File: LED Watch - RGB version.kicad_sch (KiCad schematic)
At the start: 186 parts, among them Q1 BD135, Q10 BD135, Q11 BD135, Q12 BD135, Q13 BD135, Q2 BD135, Q3 BD135, Q4 BD135, Q5 BD135, Q6 BD135, Q7 BD135, Q8 BD135, Q9 BD135, U1 ATMEGA32U4-AU, U10 74LVC2G08, U11 74LVC2G08, U12 74LVC2G08, U13 74LVC2G08, U14 74LVC2G08, U15 74LVC2G08, U16 74LVC2G08, U17 74LVC2G08, U18 74LVC2G08, U19 74LVC2G08, U2 74LVC2G08, U20 74LVC2G08, U21 74LVC2G08, U22 74LVC2G08, U23 74LVC2G08, U24 74LVC2G08, U25 74LVC2G08, U26 74LVC2G08, U27 74LVC2G08, U28 74LVC2G08, U29 74LVC2G08, U3 74LVC2G08, U30 74LVC2G08, U31 74LVC2G08, U32 74LVC2G08, U33 74LVC2G08, U34 74LVC2G08, U35 74LVC2G08, U36 74LVC2G08, U37 74LVC2G08, U38 74LVC2G08, U39 74LVC2G08, U4 74LVC2G08, U40 74LVC2G08, U41 74LVC2G08, U5 74LVC2G08, U6 74LVC2G08, U7 74LVC2G08, U8 74LVC2G08, U9 74LVC2G08

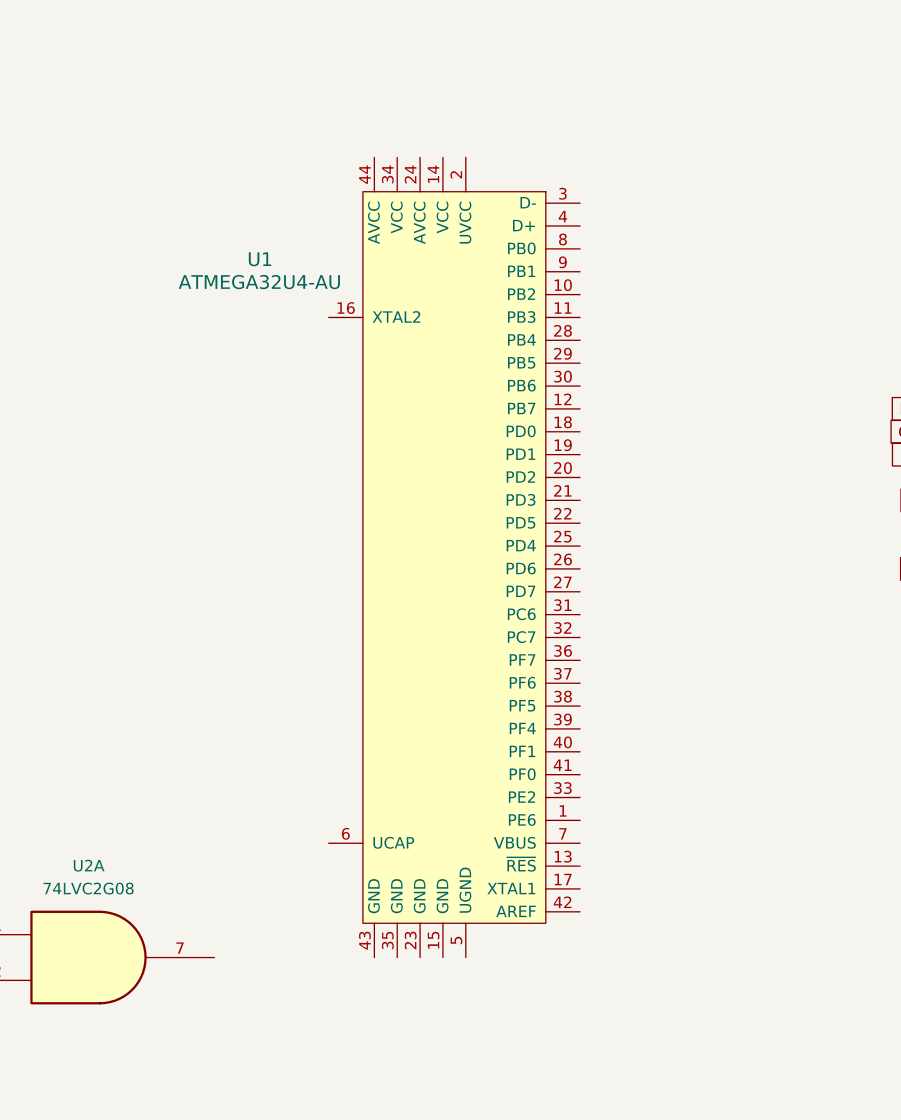
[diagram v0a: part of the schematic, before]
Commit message: chip swap to atmega4808
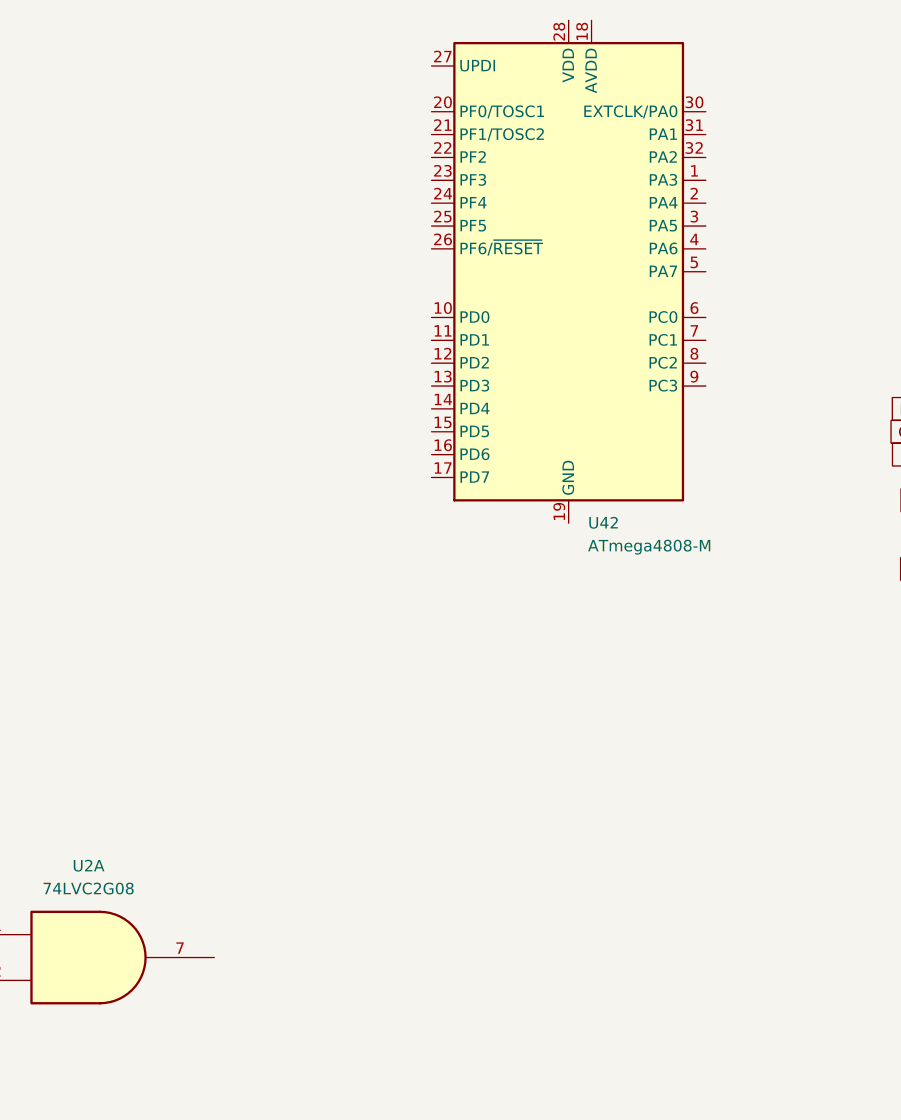
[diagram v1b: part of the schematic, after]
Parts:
- removed U1: ATMEGA32U4-AU, digikey-footprints:TQFP-44_10x10mm, symbol dk_Embedded-Microcontrollers:ATMEGA32U4-AU
- added U42: ATmega4808-M, Package_DFN_QFN:QFN-32-1EP_5x5mm_P0.5mm_EP3.1x3.1mm_ThermalVias, symbol MCU_Microchip_ATmega:ATmega4808-M
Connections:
- new net: U42.19 (GND), U42.29 (GND), U42.33 (GND)
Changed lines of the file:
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@@
 	)
 	(symbol
-		(lib_id "dk_Embedded-Microcontrollers:ATMEGA32U4-AU")
-		(at 74.93 104.14 0)
-		(mirror y)
-		(unit 1)
-		(exclude_from_sim no)
-		(in_bom yes)
-		(on_board yes)
-		(dnp no)
-		(property "Reference" "U1"
-			(at 54.61 77.3998 0)
-			(effects
-				(font
-					(size 1.524 1.524)
-				)
-			)
-		)
-		(property "Value" "ATMEGA32U4-AU"
-			(at 54.61 79.9398 0)
-			(effects
-				(font
-					(size 1.524 1.524)
-				)
-			)
-		)
-		(property "Footprint" "digikey-footprints:TQFP-44_10x10mm"
-			(at 69.85 99.06 0)
-			(effects
-				(font
-					(size 1.524 1.524)
-				)
-				(justify left)
-				(hide yes)
-			)
-		)
-		(property "Datasheet" "http://ww1.microchip.com/downloads/en/DeviceDoc/Atmel-7766-8-bit-AVR-ATmega16U4-32U4_Summary.pdf"
-			(at 69.85 96.52 0)
-			(effects
-				(font
-					(size 1.524 1.524)
-				)
-				(justify left)
-				(hide yes)
-			)
-		)
-		(property "Description" "IC MCU 8BIT 32KB FLASH 44TQFP"
-			(at 74.93 104.14 0)
-			(effects
-				(font
-					(size 1.27 1.27)
-				)
-				(hide yes)
-			)
-		)
-		(property "Digi-Key_PN" "ATMEGA32U4-AU-ND"
-			(at 69.85 93.98 0)
-			(effects
-				(font
-					(size 1.524 1.524)
-				)
-				(justify left)
-				(hide yes)
-			)
-		)
-		(property "MPN" "ATMEGA32U4-AU"
-			(at 69.85 91.44 0)
-			(effects
-				(font
-					(size 1.524 1.524)
-				)
-				(justify left)
-				(hide yes)
-			)
-		)
-		(property "Category" "Integrated Circuits (ICs)"
-			(at 69.85 88.9 0)
-			(effects
-				(font
-					(size 1.524 1.524)
-				)
-				(justify left)
-				(hide yes)
-			)
-		)
-		(property "Family" "Embedded - Microcontrollers"
-			(at 69.85 86.36 0)
-			(effects
-				(font
-					(size 1.524 1.524)
-				)
-				(justify left)
-				(hide yes)
-			)
-		)
-		(property "DK_Datasheet_Link" "http://ww1.microchip.com/downloads/en/DeviceDoc/Atmel-7766-8-bit-AVR-ATmega16U4-32U4_Summary.pdf"
-			(at 69.85 83.82 0)
-			(effects
-				(font
-					(size 1.524 1.524)
-				)
-				(justify left)
-				(hide yes)
-			)
-		)
-		(property "DK_Detail_Page" "/product-detail/en/microchip-technology/ATMEGA32U4-AU/ATMEGA32U4-AU-ND/1914602"
-			(at 69.85 81.28 0)
-			(effects
-				(font
-					(size 1.524 1.524)
-				)
-				(justify left)
-				(hide yes)
-			)
-		)
-		(property "Description_1" "IC MCU 8BIT 32KB FLASH 44TQFP"
-			(at 69.85 78.74 0)
-			(effects
-				(font
-					(size 1.524 1.524)
-				)
-				(justify left)
-				(hide yes)
-			)
-		)
-		(property "Manufacturer" "Microchip Technology"
-			(at 69.85 76.2 0)
-			(effects
-				(font
-					(size 1.524 1.524)
-				)
-				(justify left)
-				(hide yes)
-			)
-		)
-		(property "Status" "Active"
-			(at 69.85 73.66 0)
-			(effects
-				(font
-					(size 1.524 1.524)
-				)
-				(justify left)
-				(hide yes)
-			)
-		)
-		(pin "18"
-		)
-		(pin "3"
-		)
-		(pin "11"
-		)
-		(pin "8"
-		)
-		(pin "28"
-		)
-		(pin "4"
-		)
-		(pin "29"
-		)
-		(pin "30"
-		)
-		(pin "9"
-		)
-		(pin "10"
-		)
-		(pin "12"
-		)
-		(pin "41"
-		)
-		(pin "13"
-		)
-		(pin "26"
-		)
-		(pin "36"
-		)
-		(pin "22"
-		)
-		(pin "31"
-		)
-		(pin "19"
-		)
-		(pin "21"
-		)
-		(pin "20"
-		)
-		(pin "27"
-		)
-		(pin "32"
-		)
-		(pin "38"
-		)
-		(pin "40"
-		)
-		(pin "7"
-		)
-		(pin "24"
-		)
-		(pin "39"
-		)
-		(pin "14"
-		)
-		(pin "5"
-		)
-		(pin "25"
-		)
-		(pin "37"
-		)
-		(pin "33"
-		)
-		(pin "1"
-		)
-		(pin "42"
-		)
-		(pin "44"
-		)
-		(pin "35"
-		)
-		(pin "2"
-		)
-		(pin "43"
-		)
-		(pin "23"
-		)
-		(pin "16"
-		)
-		(pin "15"
-		)
-		(pin "17"
-		)
-		(pin "34"
-		)
-		(pin "6"
-		)
-		(instances
-			(project ""
-				(path "/4f6e3ccb-61a7-41db-9176-b9c2e62eec38"
-					(reference "U1")
-					(unit 1)
-				)
-			)
-		)
-	)
-	(symbol
 		(lib_id "dk_LED-Indication-Discrete:LTST-C19HE1WT")
 		(at 281.94 134.62 0)
@@
 					(unit 1)
 				)
+			)
+		)
+	)
+	(symbol
+		(lib_id "MCU_Microchip_ATmega:ATmega4808-M")
+		(at 88.9 78.74 0)
+		(unit 1)
+		(exclude_from_sim no)
+		(in_bom yes)
+		(on_board yes)
+		(dnp no)
+		(fields_autoplaced yes)
+		(property "Reference" "U42"
+			(at 91.0433 106.68 0)
+			(effects
+				(font
+					(size 1.27 1.27)
+				)
+				(justify left)
+			)
+		)
+		(property "Value" "ATmega4808-M"
+			(at 91.0433 109.22 0)
+			(effects
+				(font
+					(size 1.27 1.27)
+				)
+				(justify left)
+			)
+		)
+		(property "Footprint" "Package_DFN_QFN:QFN-32-1EP_5x5mm_P0.5mm_EP3.1x3.1mm_ThermalVias"
+			(at 88.9 78.74 0)
+			(effects
+				(font
+					(size 1.27 1.27)
+					(italic yes)
+				)
+				(hide yes)
+			)
+		)
+		(property "Datasheet" "http://ww1.microchip.com/downloads/en/DeviceDoc/40002017A.pdf"
+			(at 88.9 78.74 0)
+			(effects
+				(font
+					(size 1.27 1.27)
+				)
+				(hide yes)
+			)
+		)
+		(property "Description" "20MHz, 48kB Flash, 6kB SRAM, 256B EEPROM, VQFN-32"
+			(at 88.9 78.74 0)
+			(effects
+				(font
+					(size 1.27 1.27)
+				)
+				(hide yes)
+			)
+		)
+		(pin "28"
+		)
+		(pin "10"
+		)
+		(pin "15"
+		)
+		(pin "23"
+		)
+		(pin "17"
+		)
+		(pin "27"
+		)
+		(pin "26"
+		)
+		(pin "11"
+		)
+		(pin "16"
+		)
+		(pin "21"
+		)
+		(pin "25"
+		)
+		(pin "13"
+		)
+		(pin "12"
+		)
+		(pin "4"
+		)
+		(pin "22"
+		)
+		(pin "24"
+		)
+		(pin "20"
+		)
+		(pin "14"
+		)
+		(pin "18"
+		)
+		(pin "5"
+		)
+		(pin "30"
+		)
+		(pin "19"
+		)
+		(pin "31"
+		)
+		(pin "32"
+		)
+		(pin "1"
+		)
+		(pin "6"
+		)
+		(pin "33"
+		)
+		(pin "3"
+		)
+		(pin "8"
+		)
+		(pin "7"
+		)
+		(pin "29"
+		)
+		(pin "2"
+		)
+		(pin "9"
+		)
+		(instances
+			(project ""
+				(path "/4f6e3ccb-61a7-41db-9176-b9c2e62eec38"
+					(reference "U42")
+					(unit 1)
+				)

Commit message: added bus bars. things are where i think they should be but i need to double check transistors and do a lot more
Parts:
- removed Q1, Q10, Q11, Q12, Q13, Q2, Q3, Q4, Q5, Q6, Q7, Q8, Q9: BD135, Package_TO_SOT_THT:TO-126-3_Vertical, symbol Transistor_BJT:BD135
- removed RGB_LED126, RGB_LED127, RGB_LED128, RGB_LED129, RGB_LED138, RGB_LED139, RGB_LED140, RGB_LED141: LTST-C19HE1WT, digikey-footprints:LED_Dual0603, symbol dk_LED-Indication-Discrete:LTST-C19HE1WT
- removed U10, U11, U12, U13, U14, U15, U16, U17, U18, U19, U2, U20, U21, U22, U23, U24, U25, U26, U27, U28, U29, U3, U30, U31, U32, U33, U34, U35, U36, U37, U38, U39, U4, U40, U41, U5, U6, U7, U8, U9: 74LVC2G08, symbol 74xGxx:74LVC2G08
- removed U42: ATmega4808-M, Package_DFN_QFN:QFN-32-1EP_5x5mm_P0.5mm_EP3.1x3.1mm_ThermalVias, symbol MCU_Microchip_ATmega:ATmega4808-M
- added Q23, Q24, Q25, Q26, Q27, Q28, Q29, Q30, Q31, Q32, Q33, Q34, Q35, Q36, Q37, Q38, Q39, Q40, Q41, Q42, Q43, Q44: BD135, Package_TO_SOT_THT:TO-126-3_Vertical, symbol Transistor_BJT:BD135
- added RGB_LED10, RGB_LED3, RGB_LED6, RGB_LED7, RGB_LED8, RGB_LED9, RGB_LED94, RGB_LED95: LTST-C19HE1WT, digikey-footprints:LED_Dual0603, symbol dk_LED-Indication-Discrete:LTST-C19HE1WT
- added U1: ATmega165PA-A, Package_QFP:TQFP-64_14x14mm_P0.8mm, symbol MCU_Microchip_ATmega:ATmega165PA-A
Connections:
- net VCC: now also Q23.3 (B), Q24.3 (B), Q25.3 (B), Q26.3 (B), Q27.3 (B), Q28.3 (B), Q29.3 (B), Q30.3 (B), Q31.3 (B), Q32.3 (B), Q33.3 (B), Q34.3 (B), Q35.3 (B), Q36.3 (B), Q37.3 (B), Q38.3 (B), Q39.3 (B), Q40.3 (B), Q41.3 (B), Q42.3 (B), Q43.3 (B), Q44.3 (B)
- net at RGB_LED22.4, RGB_LED23.4, RGB_LED34.4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: now also Q36.2 (C); no longer RGB_LED58.4, RGB_LED59.4, RGB_LED70.4, RGB_LED71.4
- net R4: now reaches RGB_LED51.1 (R)
- net R4: now also RGB_LED111.1 (R), RGB_LED115.1 (R), RGB_LED119.1 (R), RGB_LED123.1 (R), RGB_LED135.1 (R), RGB_LED15.1 (R), RGB_LED21.1 (R), RGB_LED27.1 (R), RGB_LED35.1 (R), RGB_LED39.1 (R), RGB_LED43.1 (R), RGB_LED57.1 (R), RGB_LED63.1 (R), RGB_LED69.1 (R), RGB_LED75.1 (R), RGB_LED81.1 (R), RGB_LED83.1 (R), RGB_LED87.1 (R), RGB_LED99.1 (R), RGB_LED8.1 (R), RGB_LED95.1 (R), U1.11 (PB1)
- net G4: now reaches RGB_LED51.2 (G)
- net G4: now also RGB_LED111.2 (G), RGB_LED115.2 (G), RGB_LED119.2 (G), RGB_LED123.2 (G), RGB_LED135.2 (G), RGB_LED15.2 (G), RGB_LED21.2 (G), RGB_LED27.2 (G), RGB_LED35.2 (G), RGB_LED39.2 (G), RGB_LED43.2 (G), RGB_LED57.2 (G), RGB_LED63.2 (G), RGB_LED69.2 (G), RGB_LED75.2 (G), RGB_LED81.2 (G), RGB_LED83.2 (G), RGB_LED87.2 (G), RGB_LED99.2 (G), RGB_LED8.2 (G), RGB_LED95.2 (G), U1.12 (PB2)
- net B4: now reaches RGB_LED51.3 (B)
- net B4: now also RGB_LED111.3 (B), RGB_LED115.3 (B), RGB_LED119.3 (B), RGB_LED123.3 (B), RGB_LED135.3 (B), RGB_LED15.3 (B), RGB_LED21.3 (B), RGB_LED27.3 (B), RGB_LED35.3 (B), RGB_LED39.3 (B), RGB_LED43.3 (B), RGB_LED57.3 (B), RGB_LED63.3 (B), RGB_LED69.3 (B), RGB_LED75.3 (B), RGB_LED81.3 (B), RGB_LED83.3 (B), RGB_LED87.3 (B), RGB_LED99.3 (B), RGB_LED8.3 (B), RGB_LED95.3 (B), U1.13 (PB3)
- net at RGB_LED48.4, RGB_LED49.4, RGB_LED50.4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: now also Q28.2 (C); no longer RGB_LED54.4, RGB_LED55.4, RGB_LED56.4, RGB_LED57.4
- net at RGB_LED72.4, RGB_LED73.4, RGB_LED74.4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: now also Q30.2 (C); no longer RGB_LED78.4, RGB_LED79.4, RGB_LED80.4, RGB_LED81.4
- net at RGB_LED120.4, RGB_LED121.4, RGB_LED122.4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: now also Q34.2 (C)
- net R1: now reaches RGB_LED92.1 (R)
- net R1: now also RGB_LED.1 (R), RGB_LED104.1 (R), RGB_LED106.1 (R), RGB_LED108.1 (R), RGB_LED12.1 (R), RGB_LED120.1 (R), RGB_LED132.1 (R), RGB_LED18.1 (R), RGB_LED22.1 (R), RGB_LED24.1 (R), RGB_LED32.1 (R), RGB_LED36.1 (R), RGB_LED48.1 (R), RGB_LED54.1 (R), RGB_LED60.1 (R), RGB_LED66.1 (R), RGB_LED72.1 (R), RGB_LED78.1 (R), RGB_LED84.1 (R), RGB_LED96.1 (R), RGB_LED3.1 (R), U1.51 (PA0)
- net G1: now reaches RGB_LED92.2 (G)
- net G1: now also RGB_LED.2 (G), RGB_LED104.2 (G), RGB_LED106.2 (G), RGB_LED108.2 (G), RGB_LED12.2 (G), RGB_LED120.2 (G), RGB_LED132.2 (G), RGB_LED18.2 (G), RGB_LED22.2 (G), RGB_LED24.2 (G), RGB_LED32.2 (G), RGB_LED36.2 (G), RGB_LED48.2 (G), RGB_LED54.2 (G), RGB_LED60.2 (G), RGB_LED66.2 (G), RGB_LED72.2 (G), RGB_LED78.2 (G), RGB_LED84.2 (G), RGB_LED96.2 (G), RGB_LED3.2 (G), U1.50 (PA1)
- net B1: now reaches RGB_LED92.3 (B)
- net B1: now also RGB_LED.3 (B), RGB_LED104.3 (B), RGB_LED106.3 (B), RGB_LED108.3 (B), RGB_LED12.3 (B), RGB_LED120.3 (B), RGB_LED132.3 (B), RGB_LED18.3 (B), RGB_LED22.3 (B), RGB_LED24.3 (B), RGB_LED32.3 (B), RGB_LED36.3 (B), RGB_LED48.3 (B), RGB_LED54.3 (B), RGB_LED60.3 (B), RGB_LED66.3 (B), RGB_LED72.3 (B), RGB_LED78.3 (B), RGB_LED84.3 (B), RGB_LED96.3 (B), RGB_LED3.3 (B), U1.49 (PA2)
- net at RGB_LED84.4, RGB_LED85.4, RGB_LED86.4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: now also Q31.2 (C); no longer RGB_LED90.4, RGB_LED91.4, RGB_LED92.4, RGB_LED93.4
- net at RGB_LED12.4, RGB_LED13.4, RGB_LED14.4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: now also Q25.2 (C); no longer RGB_LED18.4, RGB_LED19.4, RGB_LED20.4, RGB_LED21.4
- net R5: now reaches RGB_LED112.1 (R)
- net R5: now also RGB_LED100.1 (R), RGB_LED102.1 (R), RGB_LED116.1 (R), RGB_LED124.1 (R), RGB_LED136.1 (R), RGB_LED16.1 (R), RGB_LED2.1 (R), RGB_LED28.1 (R), RGB_LED30.1 (R), RGB_LED4.1 (R), RGB_LED40.1 (R), RGB_LED44.1 (R), RGB_LED46.1 (R), RGB_LED52.1 (R), RGB_LED58.1 (R), RGB_LED64.1 (R), RGB_LED70.1 (R), RGB_LED76.1 (R), RGB_LED88.1 (R), RGB_LED90.1 (R), RGB_LED9.1 (R), U1.14 (PB4)
- net G5: now reaches RGB_LED112.2 (G)
- net G5: now also RGB_LED100.2 (G), RGB_LED102.2 (G), RGB_LED116.2 (G), RGB_LED124.2 (G), RGB_LED136.2 (G), RGB_LED16.2 (G), RGB_LED2.2 (G), RGB_LED28.2 (G), RGB_LED30.2 (G), RGB_LED4.2 (G), RGB_LED40.2 (G), RGB_LED44.2 (G), RGB_LED46.2 (G), RGB_LED52.2 (G), RGB_LED58.2 (G), RGB_LED64.2 (G), RGB_LED70.2 (G), RGB_LED76.2 (G), RGB_LED88.2 (G), RGB_LED90.2 (G), RGB_LED9.2 (G), U1.15 (PB5)
- net B5: now reaches RGB_LED112.3 (B)
- net B5: now also RGB_LED100.3 (B), RGB_LED102.3 (B), RGB_LED116.3 (B), RGB_LED124.3 (B), RGB_LED136.3 (B), RGB_LED16.3 (B), RGB_LED2.3 (B), RGB_LED28.3 (B), RGB_LED30.3 (B), RGB_LED4.3 (B), RGB_LED40.3 (B), RGB_LED44.3 (B), RGB_LED46.3 (B), RGB_LED52.3 (B), RGB_LED58.3 (B), RGB_LED64.3 (B), RGB_LED70.3 (B), RGB_LED76.3 (B), RGB_LED88.3 (B), RGB_LED90.3 (B), RGB_LED9.3 (B), U1.16 (PB6)
- net at RGB_LED108.4, RGB_LED109.4, RGB_LED110.4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: now also Q33.2 (C); no longer RGB_LED114.4, RGB_LED115.4, RGB_LED116.4, RGB_LED117.4
- net R6: now reaches RGB_LED11.1 (R)
- net R6: now also RGB_LED101.1 (R), RGB_LED103.1 (R), RGB_LED113.1 (R), RGB_LED117.1 (R), RGB_LED125.1 (R), RGB_LED137.1 (R), RGB_LED17.1 (R), RGB_LED29.1 (R), RGB_LED31.1 (R), RGB_LED41.1 (R), RGB_LED45.1 (R), RGB_LED47.1 (R), RGB_LED5.1 (R), RGB_LED53.1 (R), RGB_LED59.1 (R), RGB_LED65.1 (R), RGB_LED71.1 (R), RGB_LED77.1 (R), RGB_LED89.1 (R), RGB_LED91.1 (R), RGB_LED10.1 (R), U1.17 (PB7)
- net B2: now reaches RGB_LED1.3 (B)
- net B2: now also RGB_LED105.3 (B), RGB_LED107.3 (B), RGB_LED109.3 (B), RGB_LED121.3 (B), RGB_LED13.3 (B), RGB_LED133.3 (B), RGB_LED19.3 (B), RGB_LED23.3 (B), RGB_LED25.3 (B), RGB_LED33.3 (B), RGB_LED37.3 (B), RGB_LED49.3 (B), RGB_LED55.3 (B), RGB_LED61.3 (B), RGB_LED67.3 (B), RGB_LED73.3 (B), RGB_LED79.3 (B), RGB_LED85.3 (B), RGB_LED93.3 (B), RGB_LED97.3 (B), RGB_LED6.3 (B), U1.46 (PA5)
- net R3: now reaches RGB_LED38.1 (R)
- net R3: now also RGB_LED110.1 (R), RGB_LED114.1 (R), RGB_LED118.1 (R), RGB_LED122.1 (R), RGB_LED134.1 (R), RGB_LED14.1 (R), RGB_LED20.1 (R), RGB_LED26.1 (R), RGB_LED34.1 (R), RGB_LED42.1 (R), RGB_LED50.1 (R), RGB_LED56.1 (R), RGB_LED62.1 (R), RGB_LED68.1 (R), RGB_LED74.1 (R), RGB_LED80.1 (R), RGB_LED82.1 (R), RGB_LED86.1 (R), RGB_LED98.1 (R), RGB_LED7.1 (R), RGB_LED94.1 (R), U1.45 (PA6)
- net G3: now reaches RGB_LED38.2 (G)
- net G3: now also RGB_LED110.2 (G), RGB_LED114.2 (G), RGB_LED118.2 (G), RGB_LED122.2 (G), RGB_LED134.2 (G), RGB_LED14.2 (G), RGB_LED20.2 (G), RGB_LED26.2 (G), RGB_LED34.2 (G), RGB_LED42.2 (G), RGB_LED50.2 (G), RGB_LED56.2 (G), RGB_LED62.2 (G), RGB_LED68.2 (G), RGB_LED74.2 (G), RGB_LED80.2 (G), RGB_LED82.2 (G), RGB_LED86.2 (G), RGB_LED98.2 (G), RGB_LED7.2 (G), RGB_LED94.2 (G), U1.44 (PA7)
- net B3: now reaches RGB_LED38.3 (B)
- net B3: now also RGB_LED110.3 (B), RGB_LED114.3 (B), RGB_LED118.3 (B), RGB_LED122.3 (B), RGB_LED134.3 (B), RGB_LED14.3 (B), RGB_LED20.3 (B), RGB_LED26.3 (B), RGB_LED34.3 (B), RGB_LED42.3 (B), RGB_LED50.3 (B), RGB_LED56.3 (B), RGB_LED62.3 (B), RGB_LED68.3 (B), RGB_LED74.3 (B), RGB_LED80.3 (B), RGB_LED82.3 (B), RGB_LED86.3 (B), RGB_LED98.3 (B), RGB_LED7.3 (B), RGB_LED94.3 (B), U1.10 (PB0)
- net at RGB_LED36.4, RGB_LED37.4, RGB_LED38.4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: now also Q27.2 (C); no longer RGB_LED42.4, RGB_LED43.4, RGB_LED44.4, RGB_LED45.4
- net G6: now reaches RGB_LED11.2 (G)
- net G6: now also RGB_LED101.2 (G), RGB_LED103.2 (G), RGB_LED113.2 (G), RGB_LED117.2 (G), RGB_LED125.2 (G), RGB_LED137.2 (G), RGB_LED17.2 (G), RGB_LED29.2 (G), RGB_LED31.2 (G), RGB_LED41.2 (G), RGB_LED45.2 (G), RGB_LED47.2 (G), RGB_LED5.2 (G), RGB_LED53.2 (G), RGB_LED59.2 (G), RGB_LED65.2 (G), RGB_LED71.2 (G), RGB_LED77.2 (G), RGB_LED89.2 (G), RGB_LED91.2 (G), RGB_LED10.2 (G), U1.35 (PC0)
- net B6: now reaches RGB_LED11.3 (B)
- net B6: now also RGB_LED101.3 (B), RGB_LED103.3 (B), RGB_LED113.3 (B), RGB_LED117.3 (B), RGB_LED125.3 (B), RGB_LED137.3 (B), RGB_LED17.3 (B), RGB_LED29.3 (B), RGB_LED31.3 (B), RGB_LED41.3 (B), RGB_LED45.3 (B), RGB_LED47.3 (B), RGB_LED5.3 (B), RGB_LED53.3 (B), RGB_LED59.3 (B), RGB_LED65.3 (B), RGB_LED71.3 (B), RGB_LED77.3 (B), RGB_LED89.3 (B), RGB_LED91.3 (B), RGB_LED10.3 (B), U1.36 (PC1)
- net at RGB_LED100.4, RGB_LED101.4, RGB_LED96.4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: now also Q32.2 (C); no longer RGB_LED102.4, RGB_LED103.4, RGB_LED104.4, RGB_LED105.4
- net at RGB_LED24.4, RGB_LED25.4, RGB_LED26.4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: now also Q26.2 (C); no longer RGB_LED30.4, RGB_LED31.4, RGB_LED32.4, RGB_LED33.4
- net R2: now reaches RGB_LED23.1 (R)
- net R2: now also RGB_LED1.1 (R), RGB_LED105.1 (R), RGB_LED107.1 (R), RGB_LED109.1 (R), RGB_LED121.1 (R), RGB_LED13.1 (R), RGB_LED133.1 (R), RGB_LED19.1 (R), RGB_LED25.1 (R), RGB_LED33.1 (R), RGB_LED37.1 (R), RGB_LED49.1 (R), RGB_LED55.1 (R), RGB_LED61.1 (R), RGB_LED67.1 (R), RGB_LED73.1 (R), RGB_LED79.1 (R), RGB_LED85.1 (R), RGB_LED93.1 (R), RGB_LED97.1 (R), RGB_LED6.1 (R), U1.48 (PA3)
- net G2: now reaches RGB_LED23.2 (G)
- net G2: now also RGB_LED1.2 (G), RGB_LED105.2 (G), RGB_LED107.2 (G), RGB_LED109.2 (G), RGB_LED121.2 (G), RGB_LED13.2 (G), RGB_LED133.2 (G), RGB_LED19.2 (G), RGB_LED25.2 (G), RGB_LED33.2 (G), RGB_LED37.2 (G), RGB_LED49.2 (G), RGB_LED55.2 (G), RGB_LED61.2 (G), RGB_LED67.2 (G), RGB_LED73.2 (G), RGB_LED79.2 (G), RGB_LED85.2 (G), RGB_LED93.2 (G), RGB_LED97.2 (G), RGB_LED6.2 (G), U1.47 (PA4)
- net at RGB_LED132.4, RGB_LED133.4, RGB_LED134.4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: now also Q35.2 (C)
- net at RGB_LED106.4, RGB_LED107.4, RGB_LED11.4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: now also Q24.2 (C); no longer RGB_LED.4, RGB_LED1.4, RGB_LED4.4, RGB_LED5.4, RGB_LED82.4, RGB_LED83.4
- net at RGB_LED60.4, RGB_LED61.4, RGB_LED62.4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: now also Q29.2 (C); no longer RGB_LED66.4, RGB_LED67.4, RGB_LED68.4, RGB_LED69.4
- new net: Q41.2 (C), RGB_LED66.4, RGB_LED67.4, RGB_LED68.4, RGB_LED69.4, RGB_LED70.4, RGB_LED71.4
- new net: Q42.2 (C), RGB_LED78.4, RGB_LED79.4, RGB_LED80.4, RGB_LED81.4, RGB_LED90.4, RGB_LED91.4
- new net: Q43.2 (C), RGB_LED102.4, RGB_LED103.4, RGB_LED92.4, RGB_LED93.4, RGB_LED94.4, RGB_LED95.4
- new net: Q44.2 (C), RGB_LED104.4, RGB_LED105.4, RGB_LED114.4, RGB_LED115.4, RGB_LED116.4, RGB_LED117.4
- new net: Q39.2 (C), RGB_LED32.4, RGB_LED33.4, RGB_LED42.4, RGB_LED43.4, RGB_LED44.4, RGB_LED45.4
- new net: Q40.2 (C), RGB_LED54.4, RGB_LED55.4, RGB_LED56.4, RGB_LED57.4, RGB_LED58.4, RGB_LED59.4
- new net: Q38.2 (C), RGB_LED18.4, RGB_LED19.4, RGB_LED20.4, RGB_LED21.4, RGB_LED30.4, RGB_LED31.4
- new net: Q37.2 (C), RGB_LED10.4, RGB_LED3.4, RGB_LED6.4, RGB_LED7.4, RGB_LED8.4, RGB_LED9.4
- new net: Q23.2 (C), RGB_LED.4, RGB_LED1.4, RGB_LED4.4, RGB_LED5.4, RGB_LED82.4, RGB_LED83.4
- new net: U1.21 (VCC), U1.52 (VCC)
- new net: U1.22 (GND), U1.53 (GND), U1.63 (GND)
- new net Hour1: Q23.1 (E), U1.37 (PC2)
- new net Hour2: Q24.1 (E), U1.38 (PC3)
- new net Minute1: Q25.1 (E), U1.39 (PC4)
- new net Minute10: Q34.1 (E), U1.32 (PD7)
- new net Minute2: Q26.1 (E), U1.40 (PC5)
- new net Minute3: Q27.1 (E), U1.41 (PC6)
- new net Minute4: Q28.1 (E), U1.42 (PC7)
- new net Minute5: Q29.1 (E), U1.27 (PD2)
- new net Minute6: Q30.1 (E), U1.28 (PD3)
- new net Minute7: Q31.1 (E), U1.29 (PD4)
- new net Minute8: Q32.1 (E), U1.30 (PD5)
- new net Minute9: Q33.1 (E), U1.31 (PD6)
- new net Second1: Q35.1 (E), U1.4 (PE2)
- new net Second10: Q44.1 (E), U1.18 (PG3)
- new net Second2: Q36.1 (E), U1.5 (PE3)
- new net Second3: Q37.1 (E), U1.6 (PE4)
- new net Second4: Q38.1 (E), U1.7 (PE5)
- new net Second5: Q39.1 (E), U1.8 (PE6)
- new net Second6: Q40.1 (E), U1.9 (PE7)
- new net Second7: Q41.1 (E), U1.33 (PG0)
- new net Second8: Q42.1 (E), U1.34 (PG1)
- new net Second9: Q43.1 (E), U1.43 (PG2)
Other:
- moved on the sheet: RGB_LED100, RGB_LED101, RGB_LED108, RGB_LED109, RGB_LED110, RGB_LED111, RGB_LED112, RGB_LED113, RGB_LED12, RGB_LED120, RGB_LED121, RGB_LED122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
